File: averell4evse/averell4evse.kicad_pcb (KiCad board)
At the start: 2 copper layers, 91 x 78 mm, 41 parts, among them J1 Conn_01x16, J2 Conn_01x12, J3 Conn_01x04, J4 Conn_01x03, J5 Conn_01x09, U1 KT2520K-T, U2 NFCv4, U3 TLC5957RTQ, U4 74AUC1G126, U5 touch_sensor

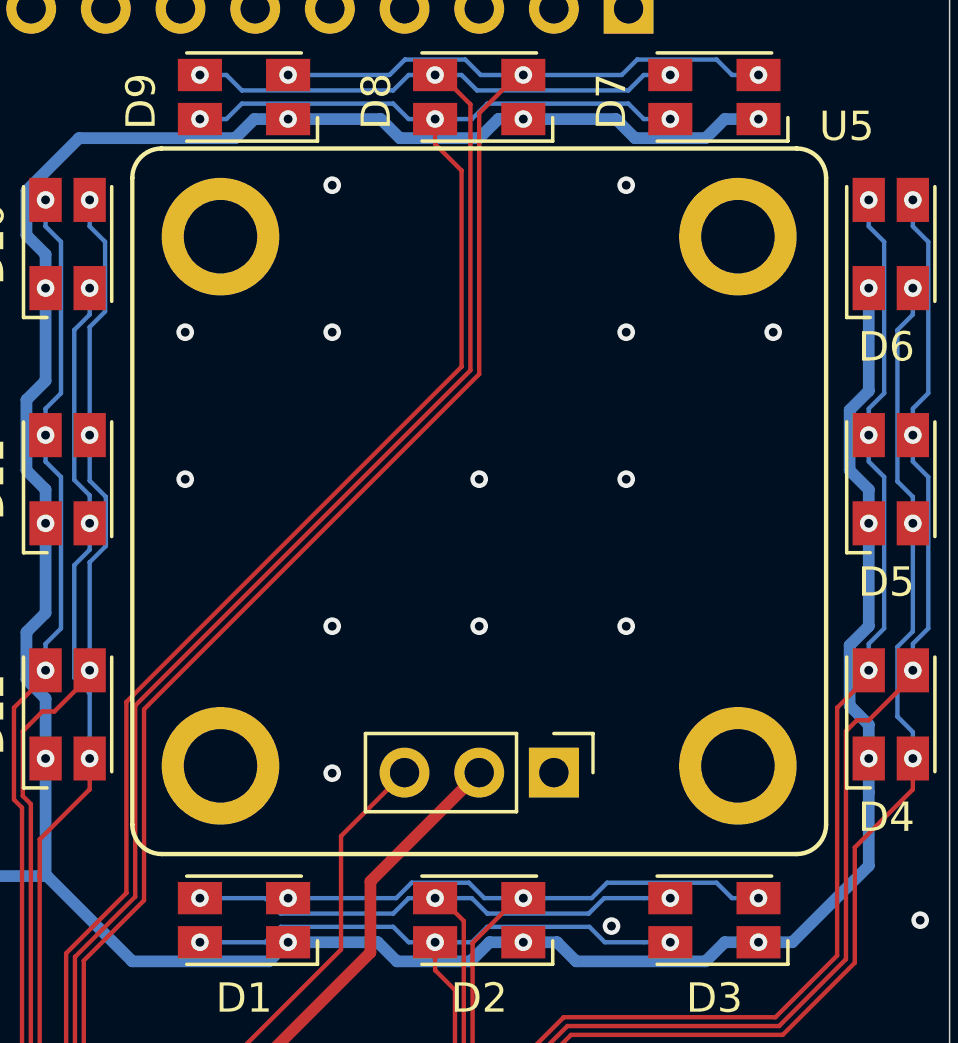
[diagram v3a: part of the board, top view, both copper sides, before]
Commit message: averell/pcb: Add ground plane keepout under the touch sensor
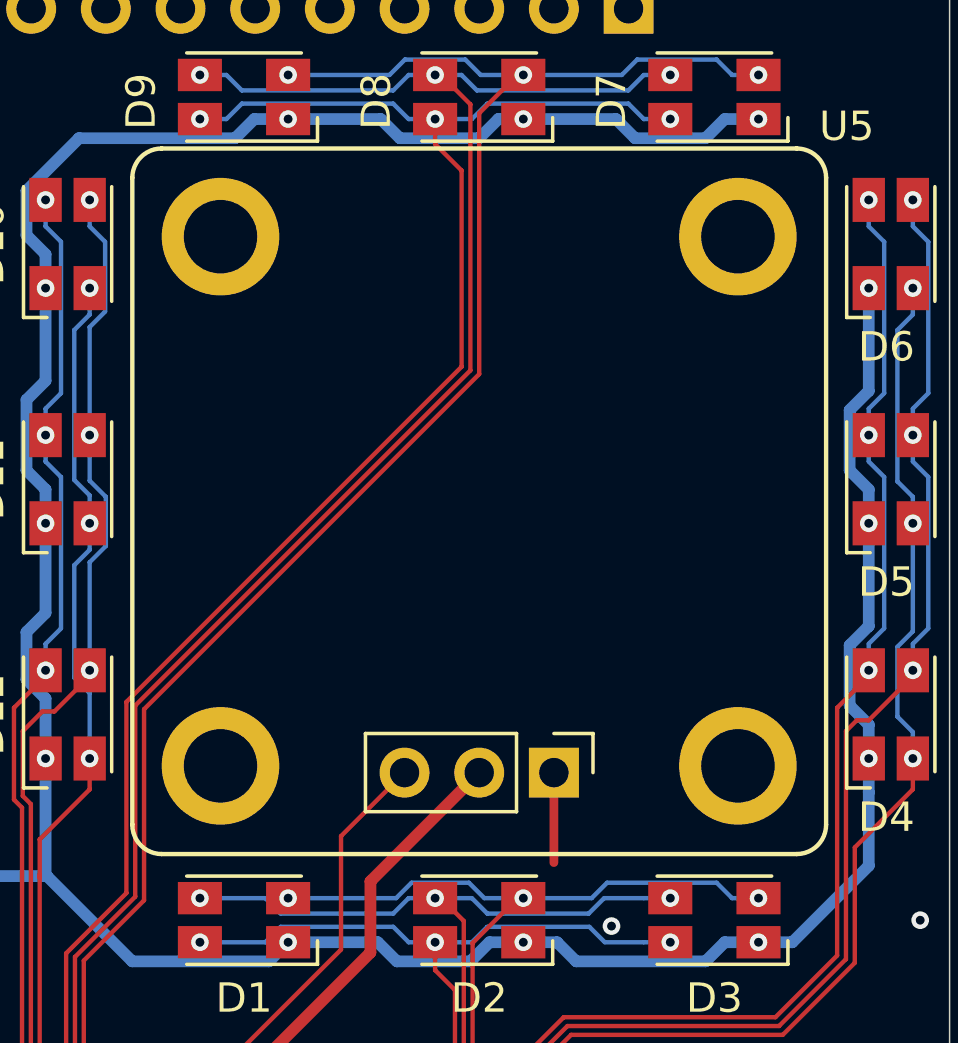
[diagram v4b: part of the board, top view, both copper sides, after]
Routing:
- net GND: track 25.9 -> 29.0 mm, vias 109 -> 98
- net (no net): vias 2 -> 0
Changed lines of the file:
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@@
     (thickness 1.6)
     (drawings 35)
-    (tracks 1137)
+    (tracks 1125)
     (zones 0)
     (modules 42)
@@
   )
   (setup
-    (last_trace_width 0.15)
+    (last_trace_width 0.3)
     (user_trace_width 0.15)
     (user_trace_width 0.25)
@@
   (gr_line (start 166 55) (end 166 125) (layer Edge.Cuts) (width 0.05))
   (gr_line (start 79 51) (end 162 51) (layer Edge.Cuts) (width 0.05))
-  (via (at 160 70) (size 0.6) (drill 0.3) (layers F.Cu B.Cu) (net 0))
-  (via (at 145 70) (size 0.6) (drill 0.3) (layers F.Cu B.Cu) (net 0))
   (via (at 87.3 115.7) (size 0.6) (drill 0.3) (layers F.Cu B.Cu) (net 1))
   (via (at 118.4 106.5) (size 0.6) (drill 0.3) (layers F.Cu B.Cu) (net 1))
@@
   (via (at 125 65) (size 0.6) (drill 0.3) (layers F.Cu B.Cu) (net 1))
   (via (at 130 65) (size 0.6) (drill 0.3) (layers F.Cu B.Cu) (net 1))
-  (via (at 145 65) (size 0.6) (drill 0.3) (layers F.Cu B.Cu) (net 1))
-  (via (at 155 65) (size 0.6) (drill 0.3) (layers F.Cu B.Cu) (net 1))
-  (via (at 155 70) (size 0.6) (drill 0.3) (layers F.Cu B.Cu) (net 1))
   (via (at 119.7 96.6) (size 0.6) (drill 0.3) (layers F.Cu B.Cu) (net 1))
-  (via (at 140 70) (size 0.6) (drill 0.3) (layers F.Cu B.Cu) (net 1))
   (via (at 130 70) (size 0.6) (drill 0.3) (layers F.Cu B.Cu) (net 1))
   (via (at 125 70) (size 0.6) (drill 0.3) (layers F.Cu B.Cu) (net 1))
   (via (at 130 75) (size 0.6) (drill 0.3) (layers F.Cu B.Cu) (net 1))
-  (via (at 140 75) (size 0.6) (drill 0.3) (layers F.Cu B.Cu) (net 1))
-  (via (at 150 75) (size 0.6) (drill 0.3) (layers F.Cu B.Cu) (net 1))
-  (via (at 150 80) (size 0.6) (drill 0.3) (layers F.Cu B.Cu) (net 1))
-  (via (at 145 80) (size 0.6) (drill 0.3) (layers F.Cu B.Cu) (net 1))
   (via (at 125 85) (size 0.6) (drill 0.3) (layers F.Cu B.Cu) (net 1))
   (via (at 130 85) (size 0.6) (drill 0.3) (layers F.Cu B.Cu) (net 1))
-  (via (at 145 85) (size 0.6) (drill 0.3) (layers F.Cu B.Cu) (net 1))
   (via (at 165 90) (size 0.6) (drill 0.3) (layers F.Cu B.Cu) (net 1))
   (via (at 130 90) (size 0.6) (drill 0.3) (layers F.Cu B.Cu) (net 1))
@@
   (via (at 87.5 109) (size 0.6) (drill 0.3) (layers F.Cu B.Cu) (net 1))
   (via (at 94.560231 100.55001) (size 0.6) (drill 0.3) (layers F.Cu B.Cu) (net 1))
-  (via (at 155 75) (size 0.6) (drill 0.3) (layers F.Cu B.Cu) (net 1))
-  (via (at 155 80) (size 0.6) (drill 0.3) (layers F.Cu B.Cu) (net 1))
   (via (at 117.4 96.6) (size 0.6) (drill 0.3) (layers F.Cu B.Cu) (net 1))
   (segment (start 116.150001 96.450001) (end 116.3 96.6) (width 0.4) (layer B.Cu) (net 1))
@@
   (segment (start 115.812001 95.599999) (end 116.150001 95.937999) (width 0.4) (layer B.Cu) (net 1))
   (via (at 145 104.8) (size 0.6) (drill 0.3) (layers F.Cu B.Cu) (net 1))
+  (segment (start 152.54 84.98) (end 152.54 88.04) (width 0.3) (layer F.Cu) (net 1))
   (segment (start 90.57001 120.75001) (end 105.032179 120.75001) (width 0.4) (layer B.Cu) (net 2))
   (segment (start 88.82 119) (end 90.57001 120.75001) (width 0.4) (layer B.Cu) (net 2))
@@
       )
     )
+  )
+  (zone (net 0) (net_name "") (layers F&B.Cu) (hatch edge 0.508)
+    (connect_pads (clearance 0.508))
+    (min_thickness 0.254)
+    (keepout (tracks allowed) (vias allowed) (copperpour not_allowed))
+    (fill (arc_segments 32) (thermal_gap 0.508) (thermal_bridge_width 0.508))
+    (polygon
+      (pts
+        (xy 138.5 64) (xy 161.5 64) (xy 161.5 87.5) (xy 138.5 87.5)
+      )
+    )

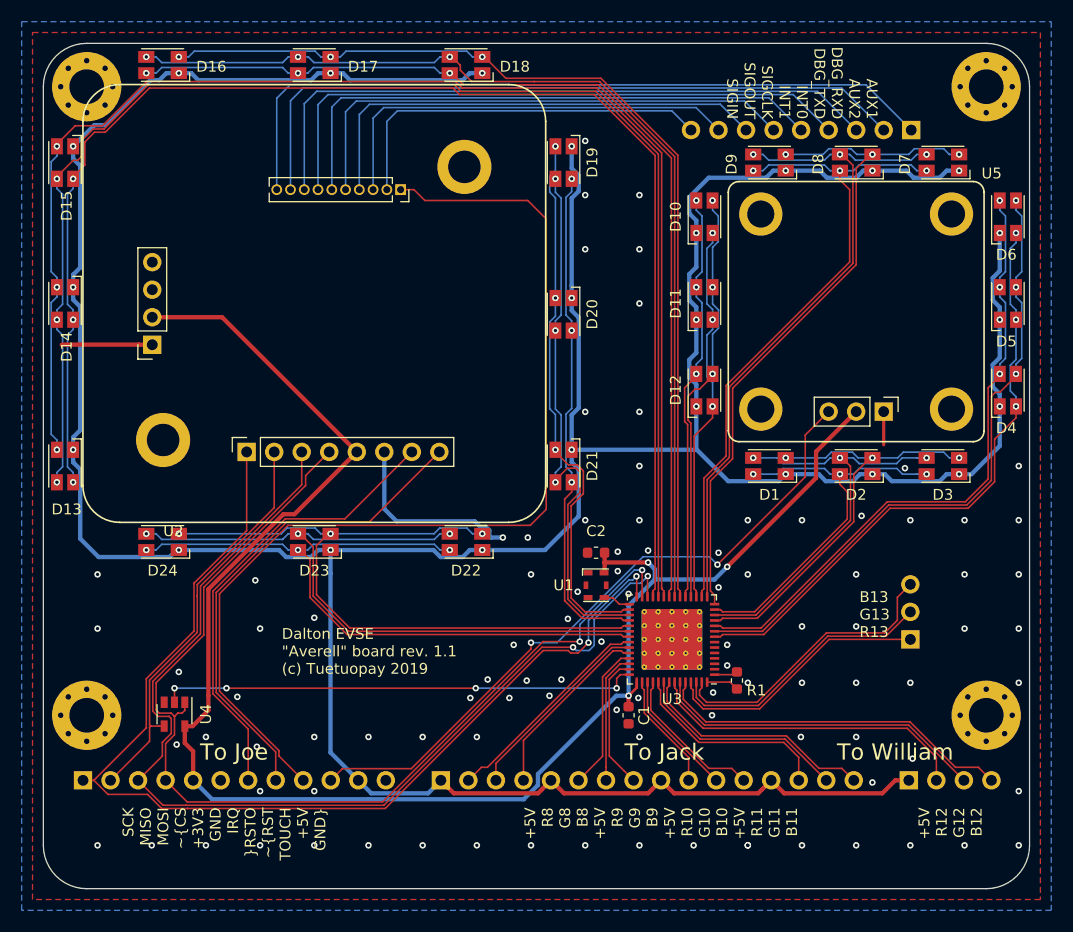
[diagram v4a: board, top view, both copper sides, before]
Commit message: averell/*: Make a real CS for LED driver
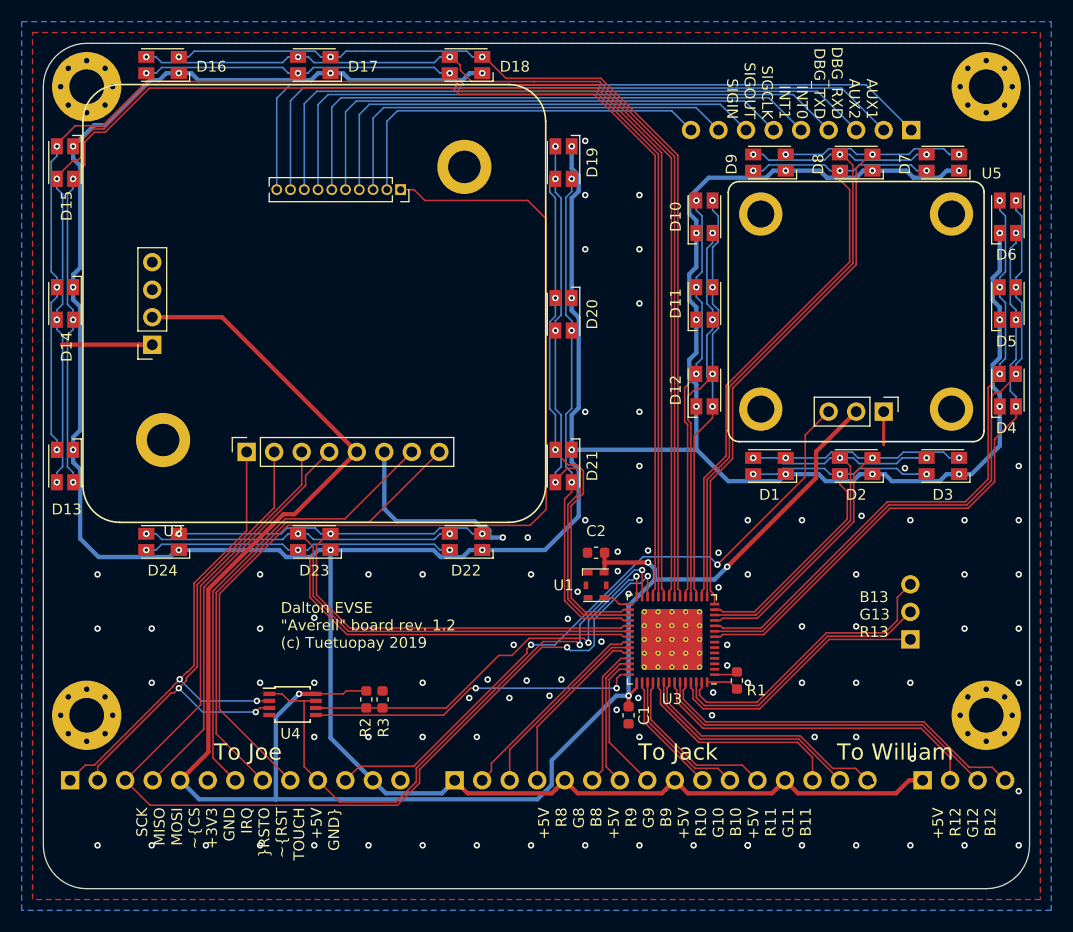
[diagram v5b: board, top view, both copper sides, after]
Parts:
- added R2: 10k, Resistor_SMD:R_0603_1608Metric, F.Cu at (104.8, 111.5)
- added R3: 10k, Resistor_SMD:R_0603_1608Metric, F.Cu at (106.3, 111.5)
- J2: value Conn_01x12 -> Conn_01x13; footprint Connector_PinHeader_2.54mm:PinHeader_1x12_P2.54mm_Horizontal -> Connector_PinHeader_2.54mm:PinHeader_1x13_P2.54mm_Horizontal
- U4: value 74AUC1G126 -> 74AUC2G125; footprint Package_TO_SOT_SMD:SOT-23-5 -> Package_SO:TSSOP-8_3x3mm_P0.65mm
- moved U4 10.9 mm to (98.0, 112.0), turned to 0 degrees
- moved J1 1.27 mm to (113.0, 119.0)
- moved J3 1.27 mm to (156.1, 119.0)
- moved J2 1.19 mm to (77.5, 119.0)
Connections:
- J2 pad 10: /TOUCH -> /DRV_CS
- J2 pad 11: +5V -> /TOUCH
- J2 pad 12: GND -> +5V
- U3 pad 27: /NFC_CS -> /DRV_CS
- U3 pad 28: /SCK -> /DRV_SCK
- U4 pad 1: /NFC_CS -> /DRV_CS
- U4 pad 2: /LED_MISO -> /SCK
- U4 pad 3: GND -> /MISO
- U4 pad 4: /MISO -> GND
- U4 pad 5: +3V3 -> /LED_MISO
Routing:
- net /NFC_CS: track 97.6 -> 37.0 mm, vias 2 -> 0
- net /DRV_CS: track 0.00 -> 56.6 mm, vias 0 -> 2
- net /SCK: track 100.4 -> 46.7 mm
- net /DRV_SCK: track 0.00 -> 38.0 mm, vias 0 -> 2
- net +3V3: track 156.1 -> 174.4 mm, vias 3 -> 4
- net /LED_MISO: track 44.3 -> 31.0 mm, vias 4 -> 2
- net /MISO: track 37.9 -> 46.6 mm, vias 0 -> 2
- net /B10: track 13.9 -> 15.7 mm
- net /G10: track 11.7 -> 13.4 mm
- net /TOUCH: track 63.3 -> 61.8 mm
- net /R11: track 19.0 -> 20.3 mm
- net /B12: track 33.2 -> 34.5 mm
- net /G12: track 30.9 -> 32.2 mm
- net /B11: track 22.1 -> 23.4 mm, vias 0 -> 1
- net /R12: track 30.1 -> 31.4 mm
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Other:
- board text added: "Dalton EVSE "Averell" board rev. 1.2 (c) Tuetuopay 2019"
- board text removed: "Dalton EVSE "Averell" board rev. 1.1 (c) Tuetuopay 2019"
